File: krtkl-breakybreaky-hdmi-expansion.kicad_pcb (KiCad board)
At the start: 2 copper layers, 0 parts

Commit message: Finished schematics, added components to PCB
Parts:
- added C1: C_100n_0402_6V3, antmicro-footprints:0402-cap, F.Cu at (155.9, 93.7)
- added C2: C_100n_0402_6V3, antmicro-footprints:0402-cap, F.Cu at (189.3, 71.5)
- added C3: C_100n_0402_6V3, antmicro-footprints:0402-cap, F.Cu at (158.8, 93.7)
- added C4: C_22u_0805, antmicro-footprints:0805-cap, F.Cu at (133.2, 81.0)
- added C5: C_10n_0402, antmicro-footprints:0402-cap, F.Cu at (144.3, 74.8)
- added C6: C_22u_0805_10V, antmicro-footprints:0805-cap, F.Cu at (121.4, 82.7)
- added C7: C_22u_0805_10V, antmicro-footprints:0805-cap, F.Cu at (204.2, 68.5)
- added C8: C_22u_0805_10V, antmicro-footprints:0805-cap, F.Cu at (121.4, 85.6)
- added D1: 1N4148WS, antmicro-footprints:SOD-323F, F.Cu at (165.6, 84.5)
- added D2: KP-1608CGCK, antmicro-footprints:LED_0603, F.Cu at (120.9, 88.3)
- added D3: KP-1608CGCK, antmicro-footprints:LED_0603, F.Cu at (125.7, 85.7)
- added D4: KP-1608CGCK, antmicro-footprints:LED_0603, F.Cu at (120.9, 90.8)
- added D5: KP-1608CGCK, antmicro-footprints:LED_0603, F.Cu at (124.7, 88.3)
- added J1: SMH-120-02-T-D, antmicro-footprints:SMH-120-02-T-D, B.Cu at (189.9, 104.5)
- added J2: 685119134923, antmicro-footprints:HDMI_A_Female_685119134923, F.Cu at (137.7, 112.5)
- added L1: XFL4020-102MEB, antmicro-footprints:XFL4020-102MEB, F.Cu at (128.9, 76.7)
- added N1: oshw_logo, antmicro-footprints:oshw-logo, F.Cu at (165.2, 106.8)
- added N2: antmicro_logo, antmicro-footprints:antmicro-logo_scaled_20mm, F.Cu at (181.1, 107.0)
- added Q1: BSS138AKA, antmicro-footprints:SOT-23-3, F.Cu at (190.2, 68.0)
- added Q2: BSS138AKA, antmicro-footprints:SOT-23-3, F.Cu at (134.1, 76.3)
- added Q3: BSS138AKA, antmicro-footprints:SOT-23-3, F.Cu at (128.4, 82.0)
- added R1: R_10k_0402, antmicro-footprints:0402-res, F.Cu at (155.9, 95.7)
- added R10: R_402k_0402, antmicro-footprints:0402-res, F.Cu at (150.1, 74.8)
- added R11: R_100k_0402, antmicro-footprints:0402-res, F.Cu at (141.4, 74.8)
- added R2: R_10k_0402, antmicro-footprints:0402-res, F.Cu at (169.1, 84.1)
- added R3: R_0R_0402, antmicro-footprints:0402-res, F.Cu at (156.0, 74.8)
- added R4: R_10k_0402, antmicro-footprints:0402-res, F.Cu at (165.0, 87.0)
- added R5: R_470R_0402, antmicro-footprints:0402-res, F.Cu at (158.9, 74.8)
- added R6: R_330R_0402, antmicro-footprints:0402-res, F.Cu at (161.8, 74.8)
- added R7: R_330R_0402, antmicro-footprints:0402-res, F.Cu at (147.2, 74.8)
- added R8: R_330R_0402, antmicro-footprints:0402-res, F.Cu at (153.1, 74.8)
- added R9: R_1M_0603, antmicro-footprints:0603-res, F.Cu at (138.2, 75.1)
- added U1: TPD12S016PWR, antmicro-footprints:TPD12S016PWR, F.Cu at (150.7, 114.7)
- added U2: TPS61232DRCT, antmicro-footprints:VSON-10-1EP_3x3mm, F.Cu at (204.2, 64.0)
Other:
- board outline added: 62.2 x 19.7 mm

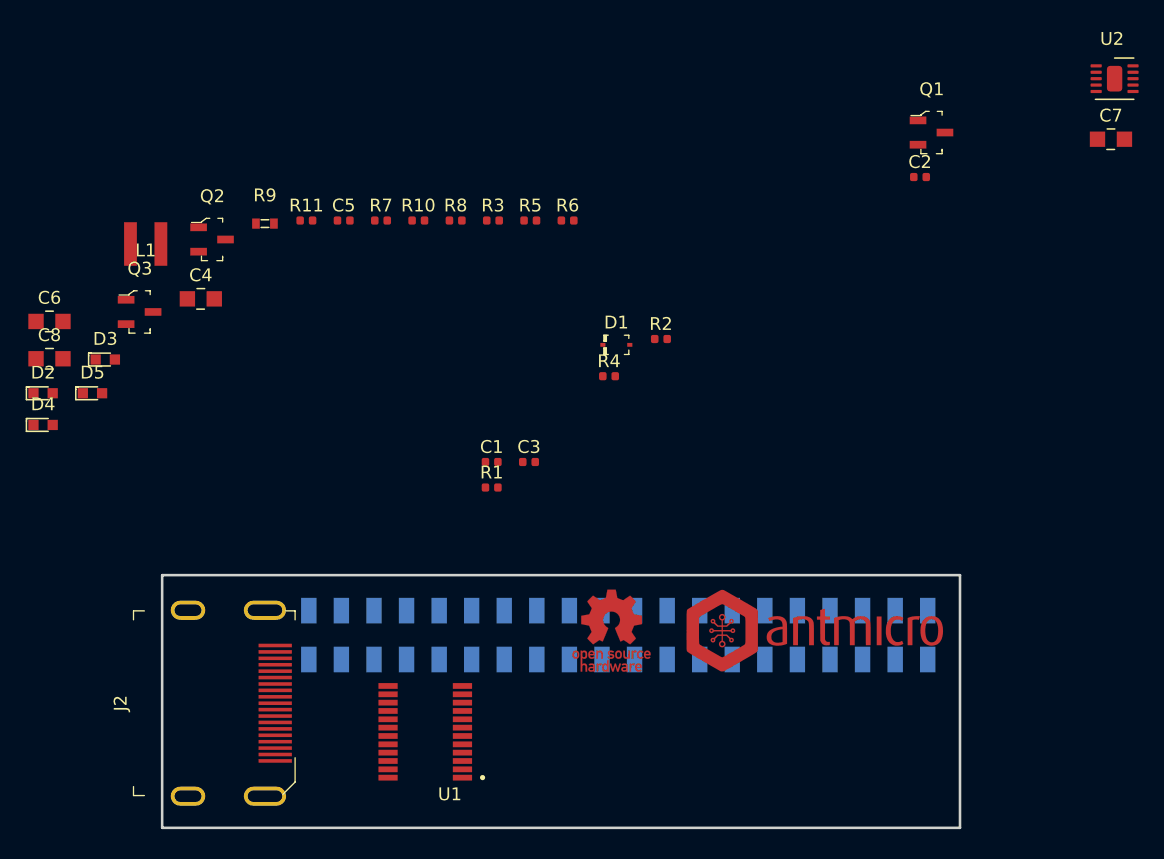
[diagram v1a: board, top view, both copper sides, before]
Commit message: Defined component placement and board stackup
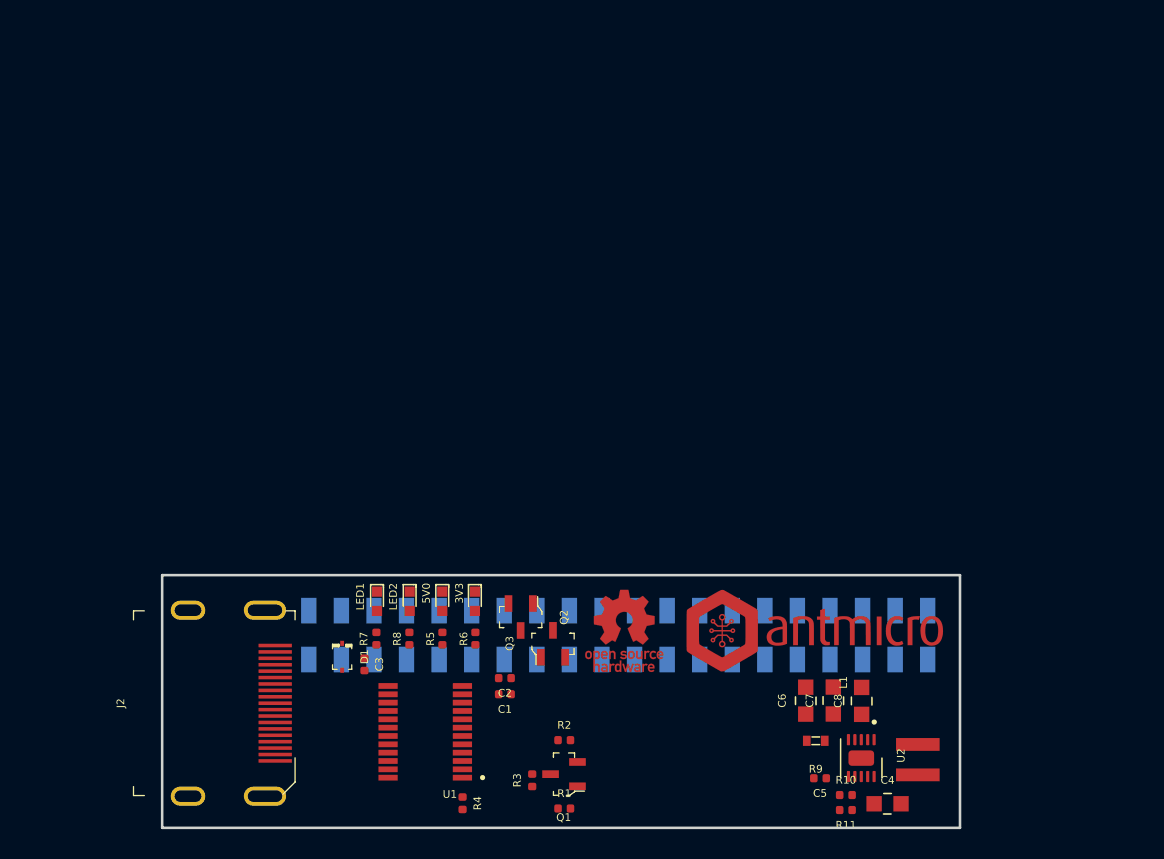
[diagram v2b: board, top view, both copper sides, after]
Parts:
- removed D5: KP-1608CGCK, antmicro-footprints:LED_0603
- added LED2: KP-1608CGCK, antmicro-footprints:LED_0603, F.Cu at (149.5, 104.5)
- moved L1 72.4 mm to (189.1, 116.9), turned to 90 degrees
- moved C8 68.7 mm to (184.7, 112.3), turned to 90 degrees
- moved C4 66.5 mm to (186.7, 120.3)
- moved C6 66.0 mm to (180.3, 112.3), turned to 90 degrees
- moved R11 62.3 mm to (183.5, 120.8), turned to 180 degrees
- moved R9 58.9 mm to (181.1, 115.4), turned to 180 degrees
- moved Q1 57.7 mm to (161.5, 118.0), turned to 180 degrees
- moved C5 57.2 mm to (181.5, 118.3), turned to 180 degrees
- moved U2 56.2 mm to (184.5, 116.6), turned to 270 degrees
- moved R10 55.8 mm to (183.5, 119.7)
- moved C2 50.7 mm to (156.9, 110.5), turned to 180 degrees
- moved C7 48.8 mm to (182.5, 112.3), turned to 90 degrees
- moved R3 43.8 mm to (159.0, 118.5), turned to 90 degrees
- moved Q3 41.3 mm to (160.6, 107.9), turned to 90 degrees
- moved Q2 38.0 mm to (158.1, 105.8), turned to 270 degrees
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- renumbered D3 to 3V3, D2 to 5V0, D4 to LED1
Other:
- copper layers 2 -> 4
- net class Default: clearance 0.2 -> 0.15; trace_width 0.25 -> 0.254; via_dia 0.8 -> 0.6; via_drill 0.4 -> 0.25
- rule trace_clearance: 0.2 -> 0.15
- rule trace_min: 0.2 -> 0.15
- rule via_min_drill: 0.3 -> 0.2
- rule via_min_size: 0.4 -> 0.2

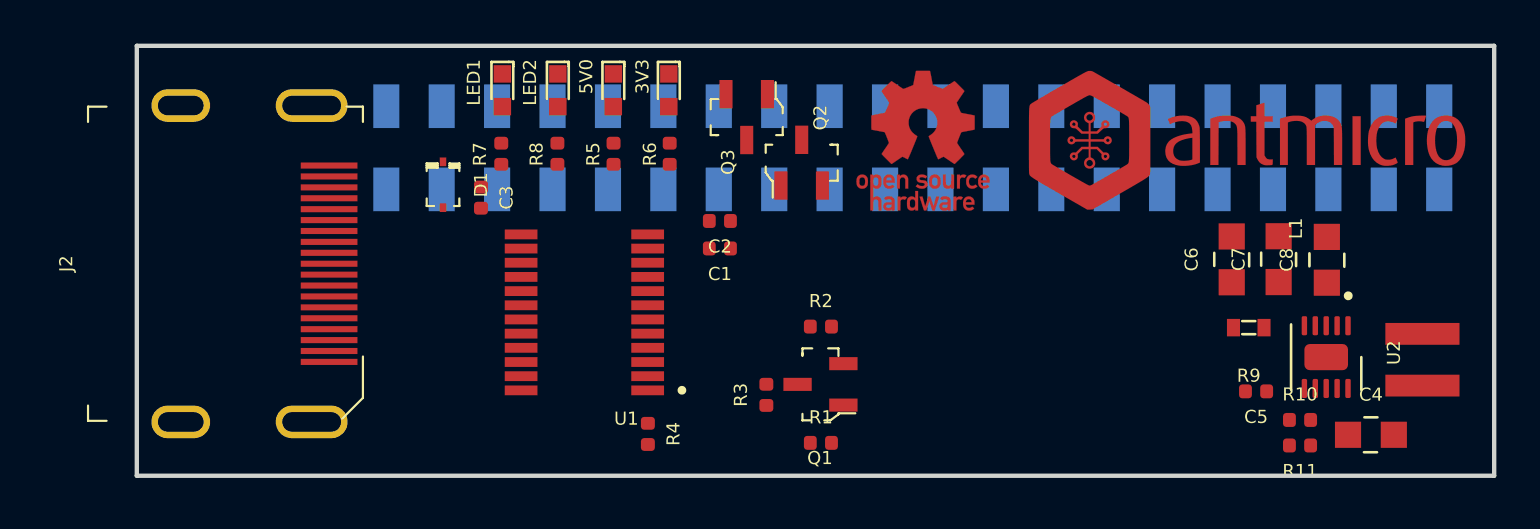
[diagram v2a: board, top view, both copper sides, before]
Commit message: PCB routed with matched length of diff-pairs
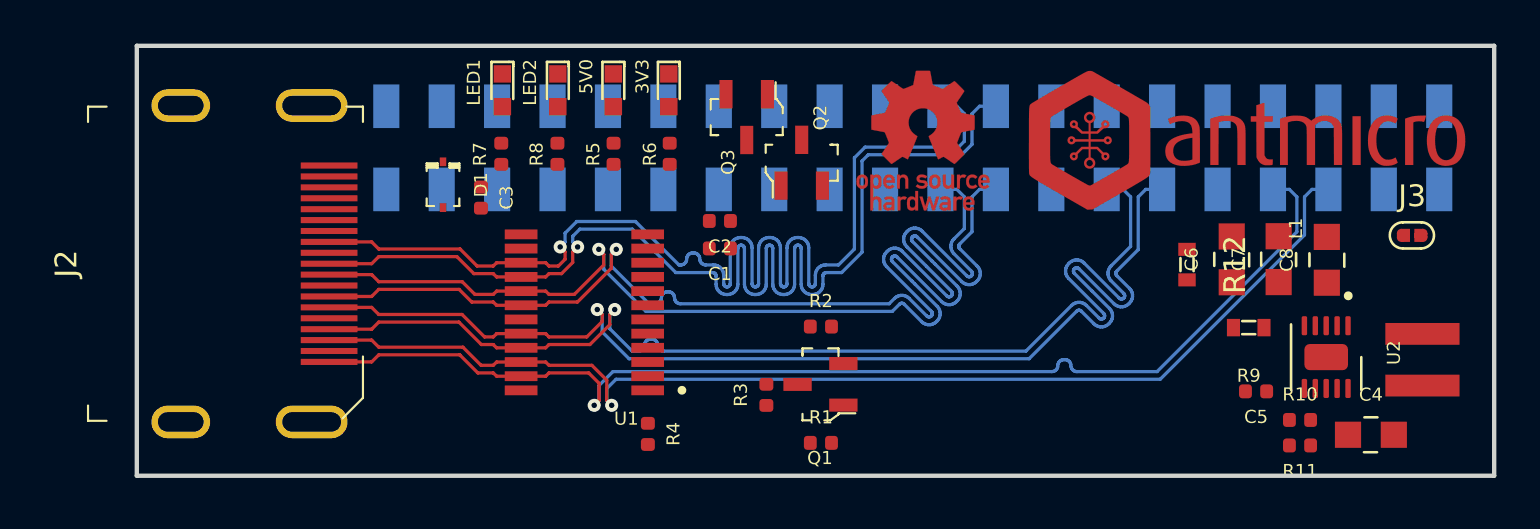
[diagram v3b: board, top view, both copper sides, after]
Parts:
- added J3: solder_jumper, antmicro-footprints:SolderJumper-0.6x1.4mm, F.Cu at (188.6, 111.2)
- added R12: R_0R_0603, antmicro-footprints:0603-res, F.Cu at (178.3, 112.5)
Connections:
- C6 pad 1: 5V0 -> Net-(C6-Pad1)
- C7 pad 1: 5V0 -> Net-(C6-Pad1)
- C8 pad 1: 5V0 -> Net-(C6-Pad1)
- J1 pad 17: /IO_L21P_T3_DQS_34 -> /TMDS_CLK_P
- J1 pad 19: /IO_L21N_T3_DQS_34 -> /TMDS_CLK_N
- J1 pad 24: /TMDS_CLK_N -> /IO_L18N_T2_34
- J1 pad 26: /TMDS_CLK_P -> /IO_L18P_T2_34
- J2 pad 11: GND -> Earth
- J2 pad 2: GND -> Earth
- J2 pad 5: GND -> Earth
- J2 pad 8: GND -> Earth
- J2 pad SH: GND -> Earth
- R10 pad 1: 5V0 -> Net-(C6-Pad1)
- R9 pad 2: 5V0 -> Net-(C6-Pad1)
- U2 pad 3: 5V0 -> Net-(C6-Pad1)
- U2 pad 4: 5V0 -> Net-(C6-Pad1)
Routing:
- net /TMDS_DATA1_P: track 0.00 -> 53.7 mm, vias 0 -> 1
- net /TMDS_DATA1_N: track 0.00 -> 53.7 mm, vias 0 -> 1
- net /TMDS_DATA2_P: track 0.00 -> 53.6 mm, vias 0 -> 1
- net /TMDS_CLK_N: track 0.00 -> 53.6 mm, vias 0 -> 1
- net /TMDS_DATA2_N: track 0.00 -> 53.6 mm, vias 0 -> 1
- net /TMDS_CLK_P: track 0.00 -> 53.6 mm, vias 0 -> 1
- net /TMDS_DATA0_P: track 0.00 -> 53.5 mm, vias 0 -> 1
- net /TMDS_DATA0_N: track 0.00 -> 53.5 mm, vias 0 -> 1

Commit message: Finished routing, minor footprint fixes
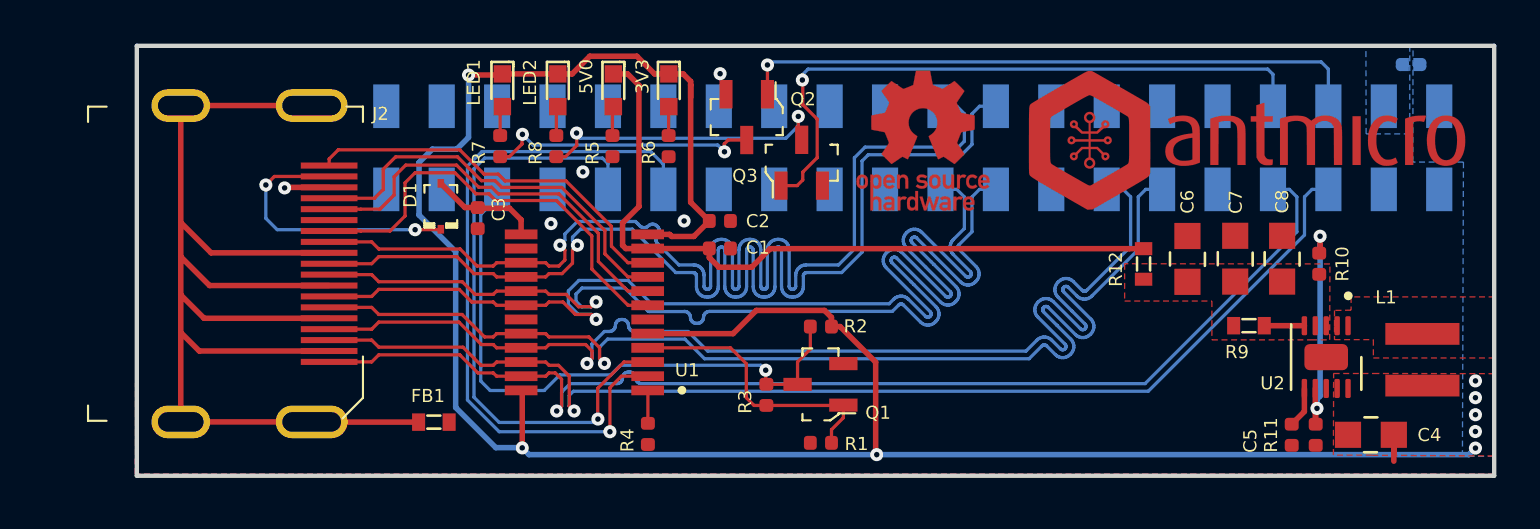
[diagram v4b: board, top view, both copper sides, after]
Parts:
- added FB1: BLM18PG121SN1D, antmicro-footprints:0603-res, F.Cu at (143.8, 119.8)
- J3: moved to B.Cu
- moved J3 7.83 mm to (188.6, 103.4)
- moved R10 7.21 mm to (184.4, 112.5), turned to 90 degrees
- moved C5 2.58 mm to (183.1, 120.3), turned to 270 degrees
- moved C8 2.05 mm to (182.7, 112.3)
- moved C6 2.03 mm to (178.3, 112.3)
- moved R12 1.99 mm to (176.3, 112.5)
- moved C7 1.99 mm to (180.5, 112.3)
- moved D1 1.00 mm to (144.1, 109.9), turned to 90 degrees
- moved C3 0.95 mm to (145.8, 110.4), turned to 90 degrees
- moved R11 0.87 mm to (184.2, 120.3), turned to 270 degrees
- moved R6 0.35 mm to (154.5, 107.1)
- moved R7 0.35 mm to (146.8, 107.1)
- moved R5 0.35 mm to (152.0, 107.1)
- moved R8 0.35 mm to (149.4, 107.1)
- moved R9 0.09 mm to (181.1, 115.3)
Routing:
- net 3V3: track 0.00 -> 105.8 mm, vias 0 -> 8
- net Earth: track 0.00 -> 60.5 mm
- net 5V0: track 0.00 -> 33.9 mm
- net /HDMI_SCL_3V3: track 0.00 -> 32.5 mm, vias 0 -> 1
- net /GP_LED2: track 0.00 -> 29.7 mm, vias 0 -> 1
- net /GP_LED1: track 0.00 -> 28.9 mm, vias 0 -> 1
- net /HDMI_SDA_3V3: track 0.00 -> 28.5 mm, vias 0 -> 1
- net /TMDS_HPD_3V3: track 0.00 -> 27.9 mm, vias 0 -> 1
- net /HDMI_CEC_5V: track 0.00 -> 20.0 mm
- net /HDMI_SCL_5V: track 0.00 -> 19.1 mm
- net /HDMI_SDA_5V: track 0.00 -> 18.8 mm
- net /HDMI_HPD_5V: track 0.00 -> 17.7 mm
- net Net-(Q3-Pad3): track 0.00 -> 13.6 mm, vias 0 -> 2
- net /HDMI_HPD_3V3: track 0.00 -> 12.9 mm
- net Net-(D1-PadK): track 0.00 -> 12.8 mm, vias 0 -> 2
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- added copper zone on B.Cu, net /VCCO_34
- added copper zone on B.Cu, net 3V3
- added copper zone on F.Cu, net 3V3
- added copper zone on B.Cu, net GND
- added copper zone on F.Cu, net GND
- added copper zone on F.Cu, net Net-(C6-Pad1)
- added copper zone on F.Cu, net Net-(L1-Pad2)
